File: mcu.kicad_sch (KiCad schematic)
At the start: 59 parts, among them J10 Micro_SD_Card, J11 Conn_01x06, J12 Conn_01x02, J14 USB_B, J8 Conn_02x05_Odd_Even, SW1 SW_Push, SW2 SW_Push, U24 REF3333, U25 LPS25HB, U26 STM32F427ZGTx, U27 USBLC6-2SC6, Y1 8MHz

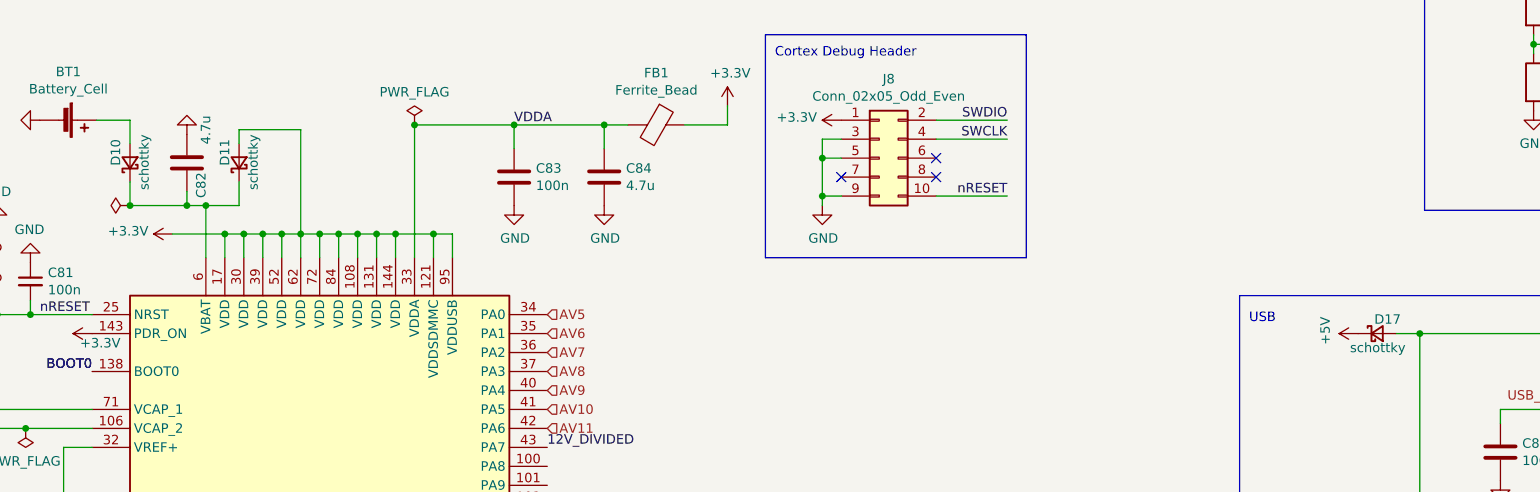
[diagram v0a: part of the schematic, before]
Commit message: USB jack, parts and LCSC numbers, headphone jack
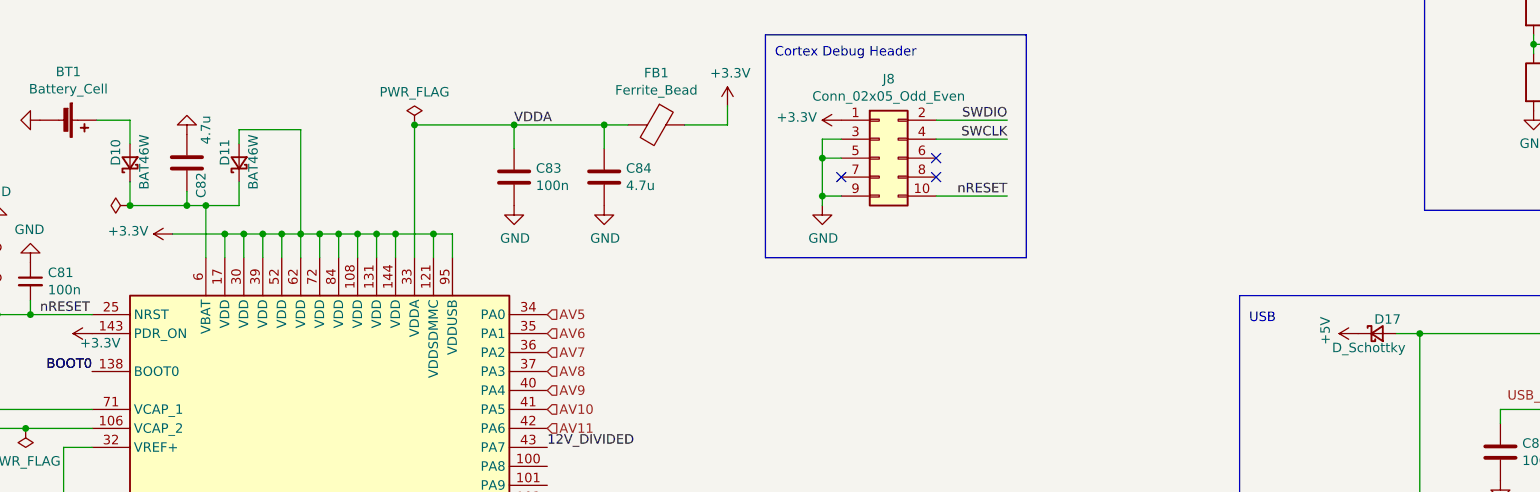
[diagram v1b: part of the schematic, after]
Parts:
- BT1: LCSC (none) -> C70377
- D10, D11: value schottky -> BAT46W; LCSC C8598 -> C83152
- D13: LCSC C2286 -> C84263
- D17: value schottky -> D_Schottky; footprint Diode_SMD:D_SOD-123 -> Diode_SMD:D_SMA; LCSC C8598 -> C8678
- J14: footprint Connector_USB:USB_B_TE_5787834_Vertical -> connector:USB_B_921-111A1010Y10200_Vertical; LCSC N/A -> C26234
- R97, R98: LCSC C11702 -> C106235
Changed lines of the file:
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@@
       (effects (font (size 1.27 1.27)) hide)
     )
-    (property "LCSC" "C2286" (at 211.455 184.15 0)
+    (property "LCSC" "C84263" (at 211.455 184.15 0)
       (effects (font (size 1.27 1.27)) hide)
     )
@@
       (effects (font (size 1.27 1.27)) (justify right))
     )
-    (property "Value" "schottky" (at 280.035 80.01 0)
+    (property "Value" "D_Schottky" (at 280.035 80.01 0)
       (effects (font (size 1.27 1.27)) (justify right))
     )
-    (property "Footprint" "Diode_SMD:D_SOD-123" (at 276.225 78.105 90)
+    (property "Footprint" "Diode_SMD:D_SMA" (at 276.225 78.105 90)
       (effects (font (size 1.27 1.27)) hide)
     )
@@
       (effects (font (size 1.27 1.27)) hide)
     )
-    (property "LCSC" "C8598" (at 276.225 78.105 0)
+    (property "LCSC" "C8678" (at 276.225 78.105 0)
       (effects (font (size 1.27 1.27)) hide)
     )
@@
       (effects (font (size 1.27 1.27)) (justify left))
     )
-    (property "Footprint" "Connector_USB:USB_B_TE_5787834_Vertical" (at 329.565 120.015 0)
+    (property "Footprint" "connector:USB_B_921-111A1010Y10200_Vertical" (at 329.565 120.015 0)
       (effects (font (size 1.27 1.27)) hide)
     )
@@
       (effects (font (size 1.27 1.27)) hide)
     )
-    (property "LCSC" "N/A" (at 329.565 120.015 0)
+    (property "LCSC" "C26234" (at 329.565 120.015 0)
       (effects (font (size 1.27 1.27)) hide)
     )
@@
       (effects (font (size 1.27 1.27)) hide)
     )
-    (property "LCSC" "C11702" (at 57.15 248.285 0)
+    (property "LCSC" "C106235" (at 57.15 248.285 0)
       (effects (font (size 1.27 1.27)) hide)
     )
@@
       (effects (font (size 1.27 1.27)) hide)
     )
-    (property "LCSC" "C11702" (at 65.405 248.285 0)
+    (property "LCSC" "C106235" (at 65.405 248.285 0)
       (effects (font (size 1.27 1.27)) hide)
     )
@@
       (effects (font (size 1.27 1.27)) (justify right))
     )
-    (property "Value" "schottky" (at 125.73 51.435 0)
+    (property "Value" "BAT46W" (at 125.73 51.435 0)
       (effects (font (size 1.27 1.27)) (justify right))
     )
@@
       (effects (font (size 1.27 1.27)) hide)
     )
-    (property "LCSC" "C8598" (at 123.825 55.245 0)
+    (property "LCSC" "C83152" (at 123.825 55.245 0)
       (effects (font (size 1.27 1.27)) hide)
     )
@@
       (effects (font (size 1.27 1.27)) (justify right))
     )
-    (property "Value" "schottky" (at 111.125 51.435 0)
+    (property "Value" "BAT46W" (at 111.125 51.435 0)
       (effects (font (size 1.27 1.27)) (justify right))
     )
@@
       (effects (font (size 1.27 1.27)) hide)
     )
-    (property "LCSC" "C8598" (at 109.22 55.245 0)
+    (property "LCSC" "C83152" (at 109.22 55.245 0)
       (effects (font (size 1.27 1.27)) hide)
     )
@@
       (effects (font (size 1.27 1.27)) hide)
     )
+    (property "LCSC" "C70377" (at 99.695 49.53 90)
+      (effects (font (size 1.27 1.27)) hide)
+    )
